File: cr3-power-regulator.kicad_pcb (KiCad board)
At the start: 2 copper layers, 25.5 x 21.1 mm, 11 parts, among them J1 Conn_01x06_Female, U1 L7812, U2 L7912

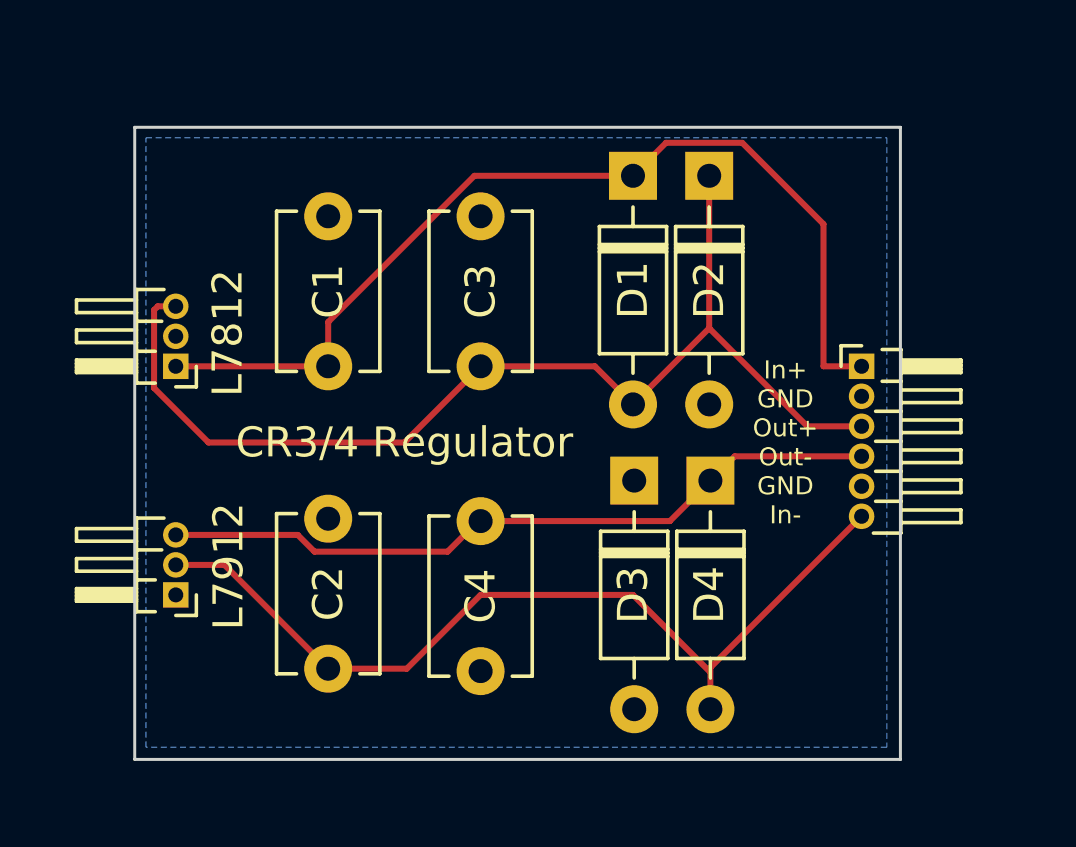
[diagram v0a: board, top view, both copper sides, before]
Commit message: Update footprints
- 1mm headder was accidentally used instead of 2.54mm (.1")
- Regulators have correct footprint
- Capacitors updated to use polarized footprints (in case it matters)
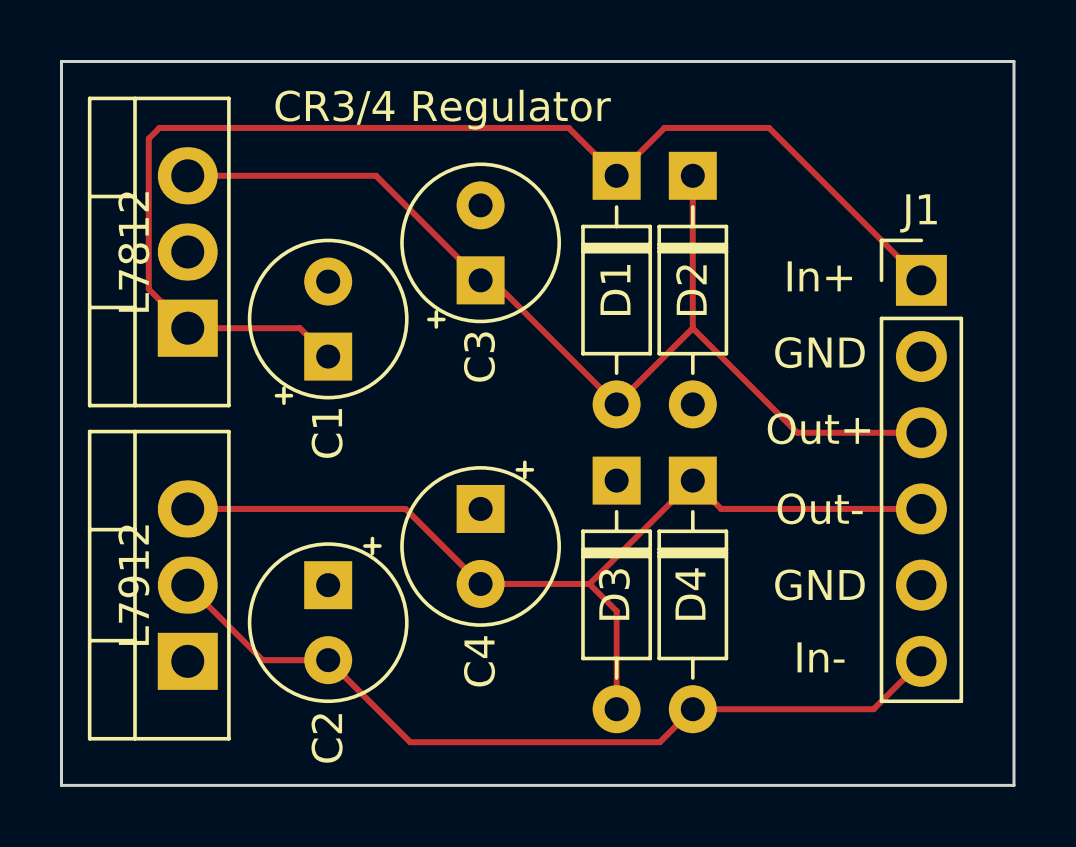
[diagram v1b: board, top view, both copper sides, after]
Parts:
- C1, C2, C3, C4: footprint Capacitor_THT:C_Disc_D5.1mm_W3.2mm_P5.00mm -> Capacitor_THT:CP_Radial_Tantal_D5.0mm_P2.50mm
- J1: footprint Connector_PinHeader_1.00mm:PinHeader_1x06_P1.00mm_Horizontal -> Connector_PinHeader_2.54mm:PinHeader_1x06_P2.54mm_Vertical
- U1, U2: footprint Connector_PinHeader_1.00mm:PinHeader_1x03_P1.00mm_Horizontal -> Package_TO_SOT_THT:TO-220-3_Vertical
- moved C4 5.40 mm to (175.3, 83.5), turned to -90 degrees
- moved J1 3.49 mm to (190.0, 75.9)
- moved C3 2.86 mm to (175.3, 75.9)
- moved U2 2.25 mm to (165.5, 88.6), turned to 90 degrees
- moved C2 2.22 mm to (170.2, 86.0)
- moved U1 1.33 mm to (165.5, 77.5), turned to 90 degrees
- moved D3 0.59 mm to (179.8, 82.5)
- moved D4 0.59 mm to (182.3, 82.5)
- moved D1 0.55 mm to (179.8, 72.4)
- moved D2 0.55 mm to (182.3, 72.4)
- moved C1 0.32 mm to (170.2, 78.4)
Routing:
- net IN_P: track 32.7 -> 41.3 mm
- net OUT_N: track 24.4 -> 31.9 mm
- net IN_N: track 29.8 -> 27.7 mm
- net OUT_P: track 36.8 -> 35.2 mm
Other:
- board size 25.5 x 21.1 mm -> 31.8 x 24.1 mm
- board text added: "GND"
- board text added: "In+"
- board text added: "In-"
- board text added: "Out+"
- board text added: "Out-"
- board text removed: "In+ GND Out+ Out- GND In-"

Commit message: Update silks
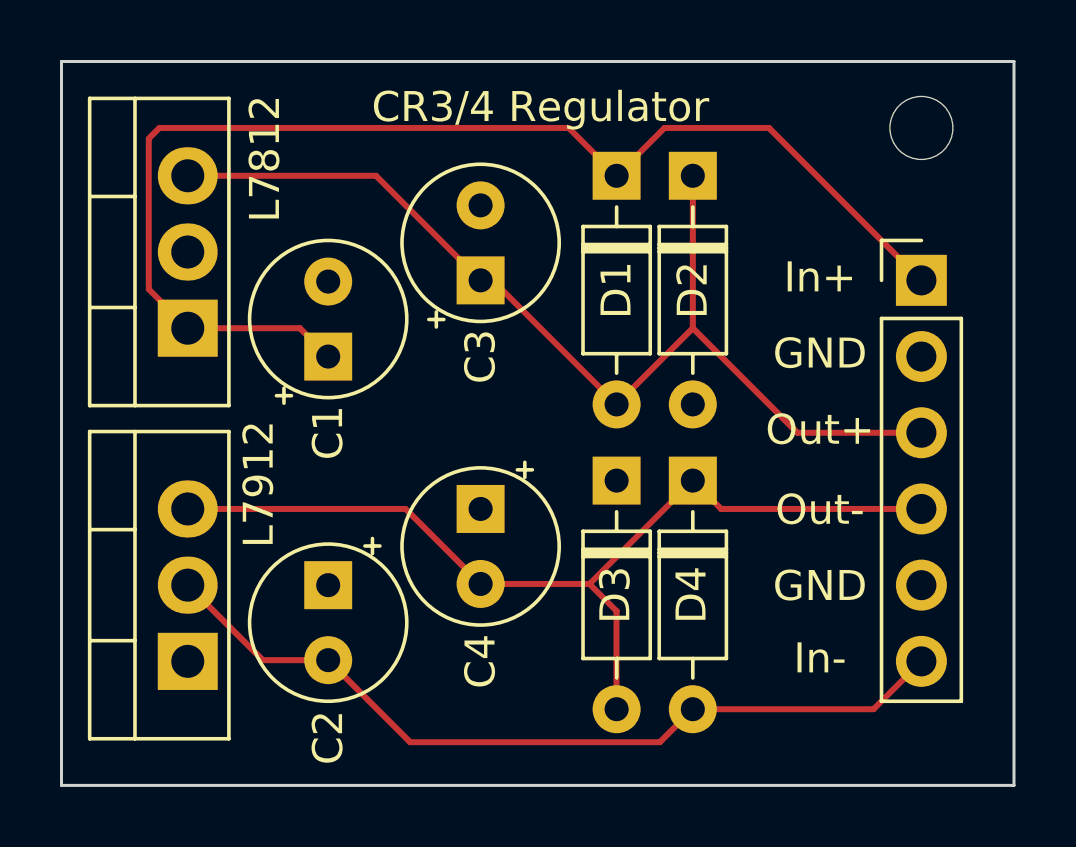
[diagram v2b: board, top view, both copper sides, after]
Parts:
- added REF**: MountingHole_2.1mm, MountingHole:MountingHole_2.1mm, F.Cu at (190.0, 70.8)
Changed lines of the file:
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@@
     (property "Sheetname" "")
     (attr through_hole)
-    (fp_text reference "J1" (at 0 -2.33) (layer "F.SilkS")
-      (effects (font (size 1 1) (thickness 0.15)))
-    )
-    (fp_text value "Conn_01x06_Female" (at -2.54 6.6675 90) (layer "F.Fab")
+    (fp_text reference "J1" (at 0 -2.33) (layer "F.SilkS") hide
+      (effects (font (size 1 1) (thickness 0.15)))
+    )
+    (fp_text value "Conn_01x06_Female" (at 2.54 6.35 90) (layer "F.Fab")
       (effects (font (size 1 1) (thickness 0.15)))
     )
@@
       (effects (font (size 1 1) (thickness 0.15)))
     )
-    (fp_text value "100n" (at 1.25 3.75 -90) (layer "F.Fab")
+    (fp_text value "100n" (at 5.08 0 -90) (layer "F.Fab")
       (effects (font (size 1 1) (thickness 0.15)))
     )
@@
     )
   )
+  (footprint "MountingHole:MountingHole_2.1mm" (layer "F.Cu")
+    (at 189.953978 70.795183)
+    (descr "Mounting Hole 2.1mm, no annular")
+    (tags "mounting hole 2.1mm no annular")
+    (attr exclude_from_pos_files exclude_from_bom)
+    (fp_text reference "REF**" (at 0 -3.2) (layer "F.SilkS") hide
+      (effects (font (size 1 1) (thickness 0.15)))
+    )
+    (fp_text value "MountingHole_2.1mm" (at 0 -2.54) (layer "F.Fab")
+      (effects (font (size 1 1) (thickness 0.15)))
+    )
+    (fp_text user "${REFERENCE}" (at 0.3 0) (layer "F.Fab")
+      (effects (font (size 1 1) (thickness 0.15)))
+    )
+    (fp_circle (center 0 0) (end 2.1 0) (layer "Cmts.User") (width 0.15) (fill none))
+    (fp_circle (center 0 0) (end 2.35 0) (layer "F.CrtYd") (width 0.05) (fill none))
+    (pad "" np_thru_hole circle locked (at 0 0) (size 2.1 2.1) (drill 2.1) (layers *.Cu *.Mask))
+  )
   (footprint "Capacitor_THT:CP_Radial_Tantal_D5.0mm_P2.50mm" (layer "F.Cu")
     (at 170.18 78.415183 90)
@@
       (effects (font (size 1 1) (thickness 0.15)))
     )
-    (fp_text value "100n" (at 1.25 3.75 90) (layer "F.Fab")
+    (fp_text value "100n" (at -2.54 0 90) (layer "F.Fab")
       (effects (font (size 1 1) (thickness 0.15)))
     )
@@
       (effects (font (size 1 1) (thickness 0.15)))
     )
-    (fp_text value "100n" (at 1.25 3.75 -90) (layer "F.Fab")
+    (fp_text value "100n" (at 5.08 0 -90) (layer "F.Fab")
       (effects (font (size 1 1) (thickness 0.15)))
     )
@@
       (effects (font (size 1 1) (thickness 0.15)))
     )
-    (fp_text value "100n" (at 1.25 3.75 90) (layer "F.Fab")
+    (fp_text value "100n" (at -2.54 0 90) (layer "F.Fab")
       (effects (font (size 1 1) (thickness 0.15)))
     )
@@
   )
   (gr_rect (start 161.29 68.58) (end 193.04 92.71) (layer "Edge.Cuts") (width 0.1) (fill none))
-  (gr_text "L7812" (at 163.738978 74.93 90) (layer "F.SilkS")
-    (effects (font (size 1 1) (thickness 0.15)))
-  )
-  (gr_text "L7912" (at 163.738978 86.035183 90) (layer "F.SilkS")
+  (gr_text "L7812" (at 168.07532 71.819615 90) (layer "F.SilkS")
+    (effects (font (size 1 1) (thickness 0.15)))
+  )
+  (gr_text "L7912" (at 167.868673 82.668594 90) (layer "F.SilkS")
     (effects (font (size 1 1) (thickness 0.15)))
   )
@@
     (effects (font (size 1 1) (thickness 0.15)))
   )
-  (gr_text "CR3/4 Regulator" (at 173.972697 70.101461) (layer "F.SilkS")
-    (effects (font (size 1 1) (thickness 0.15)))
-  )
+  (gr_text "CR3/4 Regulator" (at 177.253978 70.101461) (layer "F.SilkS")
+    (effects (font (size 1 1) (thickness 0.15)))
+  )

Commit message: Rotate caps
All capacitors are in the same orientation which should aid in assembly
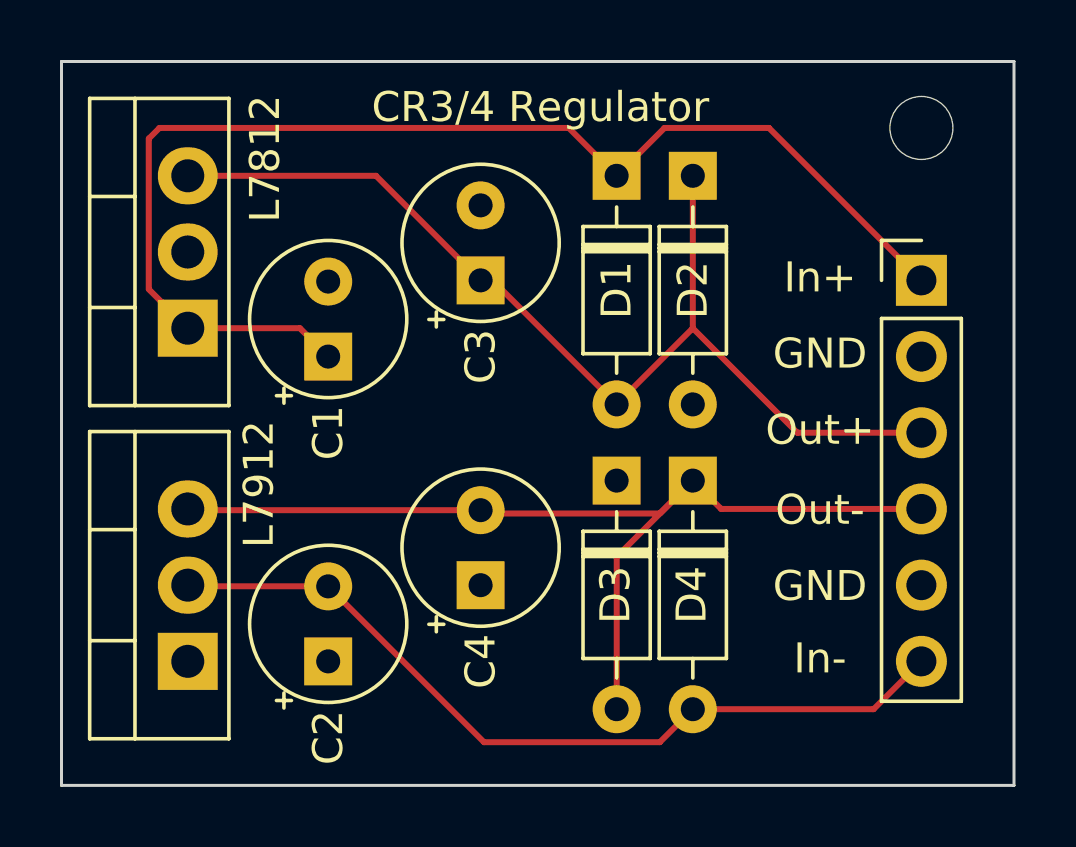
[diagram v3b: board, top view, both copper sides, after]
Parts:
- moved C4 2.54 mm to (175.3, 86.0), turned to 90 degrees
- moved C2 2.54 mm to (170.2, 88.6), turned to 90 degrees
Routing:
- net OUT_N: track 31.9 -> 34.0 mm
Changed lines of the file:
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@@
   )
   (footprint "Capacitor_THT:CP_Radial_Tantal_D5.0mm_P2.50mm" (layer "F.Cu")
-    (at 175.26 83.495183 -90)
+    (at 175.26 86.035183 90)
     (descr "CP, Radial_Tantal series, Radial, pin pitch=2.50mm, , diameter=5.0mm, Tantal Electrolytic Capacitor, http://cdn-reichelt.de/documents/datenblatt/B300/TANTAL-TB-Serie%23.pdf")
     (tags "CP Radial_Tantal series Radial pin pitch 2.50mm  diameter 5.0mm Tantal Electrolytic Capacitor")
@@
     (property "Sheetname" "")
     (attr through_hole)
-    (fp_text reference "C4" (at 5.08 0 -90) (layer "F.SilkS")
-      (effects (font (size 1 1) (thickness 0.15)))
-    )
-    (fp_text value "100n" (at 5.08 0 -90) (layer "F.Fab")
-      (effects (font (size 1 1) (thickness 0.15)))
-    )
-    (fp_text user "${REFERENCE}" (at 1.25 0 -90) (layer "F.Fab")
+    (fp_text reference "C4" (at -2.54 0 90) (layer "F.SilkS")
+      (effects (font (size 1 1) (thickness 0.15)))
+    )
+    (fp_text value "100n" (at -2.54 0 90) (layer "F.Fab")
+      (effects (font (size 1 1) (thickness 0.15)))
+    )
+    (fp_text user "${REFERENCE}" (at 1.25 0 90) (layer "F.Fab")
       (effects (font (size 1 1) (thickness 0.15)))
     )
@@
     (fp_line (start -0.883605 -1.0875) (end -0.383605 -1.0875) (layer "F.Fab") (width 0.1))
     (fp_circle (center 1.25 0) (end 3.75 0) (layer "F.Fab") (width 0.1) (fill none))
-    (pad "1" thru_hole rect locked (at 0 0 270) (size 1.6 1.6) (drill 0.8) (layers *.Cu *.Mask)
+    (pad "1" thru_hole rect locked (at 0 0 90) (size 1.6 1.6) (drill 0.8) (layers *.Cu *.Mask)
       (net 2 "GND") (pintype "passive"))
-    (pad "2" thru_hole circle locked (at 2.5 0 270) (size 1.6 1.6) (drill 0.8) (layers *.Cu *.Mask)
+    (pad "2" thru_hole circle locked (at 2.5 0 90) (size 1.6 1.6) (drill 0.8) (layers *.Cu *.Mask)
       (net 5 "OUT_N") (pintype "passive"))
     (model "${KICAD6_3DMODEL_DIR}/Capacitor_THT.3dshapes/CP_Radial_Tantal_D5.0mm_P2.50mm.wrl"
@@
   )
   (footprint "Capacitor_THT:CP_Radial_Tantal_D5.0mm_P2.50mm" (layer "F.Cu")
-    (at 170.18 86.035183 -90)
+    (at 170.18 88.575183 90)
     (descr "CP, Radial_Tantal series, Radial, pin pitch=2.50mm, , diameter=5.0mm, Tantal Electrolytic Capacitor, http://cdn-reichelt.de/documents/datenblatt/B300/TANTAL-TB-Serie%23.pdf")
     (tags "CP Radial_Tantal series Radial pin pitch 2.50mm  diameter 5.0mm Tantal Electrolytic Capacitor")
@@
     (property "Sheetname" "")
     (attr through_hole)
-    (fp_text reference "C2" (at 5.08 0 -90) (layer "F.SilkS")
-      (effects (font (size 1 1) (thickness 0.15)))
-    )
-    (fp_text value "100n" (at 5.08 0 -90) (layer "F.Fab")
-      (effects (font (size 1 1) (thickness 0.15)))
-    )
-    (fp_text user "${REFERENCE}" (at 1.25 0 -90) (layer "F.Fab")
+    (fp_text reference "C2" (at -2.54 0 90) (layer "F.SilkS")
+      (effects (font (size 1 1) (thickness 0.15)))
+    )
+    (fp_text value "100n" (at -2.54 0 90) (layer "F.Fab")
+      (effects (font (size 1 1) (thickness 0.15)))
+    )
+    (fp_text user "${REFERENCE}" (at 1.25 0 90) (layer "F.Fab")
       (effects (font (size 1 1) (thickness 0.15)))
     )
@@
     (fp_line (start -0.883605 -1.0875) (end -0.383605 -1.0875) (layer "F.Fab") (width 0.1))
     (fp_circle (center 1.25 0) (end 3.75 0) (layer "F.Fab") (width 0.1) (fill none))
-    (pad "1" thru_hole rect locked (at 0 0 270) (size 1.6 1.6) (drill 0.8) (layers *.Cu *.Mask)
+    (pad "1" thru_hole rect locked (at 0 0 90) (size 1.6 1.6) (drill 0.8) (layers *.Cu *.Mask)
       (net 2 "GND") (pintype "passive"))
-    (pad "2" thru_hole circle locked (at 2.5 0 270) (size 1.6 1.6) (drill 0.8) (layers *.Cu *.Mask)
+    (pad "2" thru_hole circle locked (at 2.5 0 90) (size 1.6 1.6) (drill 0.8) (layers *.Cu *.Mask)
       (net 3 "IN_N") (pintype "passive"))
     (model "${KICAD6_3DMODEL_DIR}/Capacitor_THT.3dshapes/CP_Radial_Tantal_D5.0mm_P2.50mm.wrl"
@@
   (segment (start 189.953978 75.875183) (end 184.873978 70.795183) (width 0.2) (layer "F.Cu") (net 1))
   (segment (start 184.873978 70.795183) (end 181.388795 70.795183) (width 0.2) (layer "F.Cu") (net 1))
-  (segment (start 170.18 88.535183) (end 167.998978 88.535183) (width 0.2) (layer "F.Cu") (net 3))
-  (segment (start 167.998978 88.535183) (end 165.498978 86.035183) (width 0.2) (layer "F.Cu") (net 3))
-  (segment (start 181.234467 91.269511) (end 172.914328 91.269511) (width 0.2) (layer "F.Cu") (net 3))
+  (segment (start 165.538978 86.075183) (end 165.498978 86.035183) (width 0.2) (layer "F.Cu") (net 3))
+  (segment (start 175.374328 91.269511) (end 170.18 86.075183) (width 0.2) (layer "F.Cu") (net 3))
+  (segment (start 170.18 86.075183) (end 165.538978 86.075183) (width 0.2) (layer "F.Cu") (net 3))
+  (segment (start 181.234467 91.269511) (end 175.374328 91.269511) (width 0.2) (layer "F.Cu") (net 3))
   (segment (start 188.359161 90.17) (end 189.953978 88.575183) (width 0.2) (layer "F.Cu") (net 3))
+  (segment (start 182.333978 90.17) (end 188.359161 90.17) (width 0.2) (layer "F.Cu") (net 3))
   (segment (start 182.333978 90.17) (end 181.234467 91.269511) (width 0.2) (layer "F.Cu") (net 3))
-  (segment (start 172.914328 91.269511) (end 170.18 88.535183) (width 0.2) (layer "F.Cu") (net 3))
-  (segment (start 182.333978 90.17) (end 188.359161 90.17) (width 0.2) (layer "F.Cu") (net 3))
   (segment (start 182.333978 77.47) (end 185.819161 80.955183) (width 0.2) (layer "F.Cu") (net 4))
   (segment (start 179.793978 80.01) (end 175.659161 75.875183) (width 0.2) (layer "F.Cu") (net 4))
@@
   (segment (start 175.659161 75.875183) (end 175.26 75.875183) (width 0.2) (layer "F.Cu") (net 4))
   (segment (start 179.793978 80.01) (end 182.333978 77.47) (width 0.2) (layer "F.Cu") (net 4))
-  (segment (start 178.888795 85.995183) (end 179.793978 86.900366) (width 0.2) (layer "F.Cu") (net 5))
-  (segment (start 172.76 83.495183) (end 165.498978 83.495183) (width 0.2) (layer "F.Cu") (net 5))
-  (segment (start 179.793978 86.900366) (end 179.793978 90.17) (width 0.2) (layer "F.Cu") (net 5))
-  (segment (start 182.333978 82.55) (end 178.888795 85.995183) (width 0.2) (layer "F.Cu") (net 5))
+  (segment (start 165.538978 83.535183) (end 165.498978 83.495183) (width 0.2) (layer "F.Cu") (net 5))
+  (segment (start 182.333978 82.55) (end 181.234467 83.649511) (width 0.2) (layer "F.Cu") (net 5))
+  (segment (start 175.26 83.535183) (end 165.538978 83.535183) (width 0.2) (layer "F.Cu") (net 5))
+  (segment (start 179.793978 85.09) (end 179.793978 90.17) (width 0.2) (layer "F.Cu") (net 5))
+  (segment (start 181.234467 83.649511) (end 175.374328 83.649511) (width 0.2) (layer "F.Cu") (net 5))
+  (segment (start 182.333978 82.55) (end 179.793978 85.09) (width 0.2) (layer "F.Cu") (net 5))
+  (segment (start 175.374328 83.649511) (end 175.26 83.535183) (width 0.2) (layer "F.Cu") (net 5))
   (segment (start 183.279161 83.495183) (end 182.333978 82.55) (width 0.2) (layer "F.Cu") (net 5))
-  (segment (start 175.26 85.995183) (end 172.76 83.495183) (width 0.2) (layer "F.Cu") (net 5))
   (segment (start 189.953978 83.495183) (end 183.279161 83.495183) (width 0.2) (layer "F.Cu") (net 5))
-  (segment (start 175.26 85.995183) (end 178.888795 85.995183) (width 0.2) (layer "F.Cu") (net 5))
   (zone (net 2) (net_name "GND") (layer "B.Cu") (hatch edge 0.508)
     (connect_pads (clearance 0.508))
